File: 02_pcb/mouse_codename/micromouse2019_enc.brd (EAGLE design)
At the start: 5.9 x 11.1 mm, 7 parts, among them IC1 AS5047D

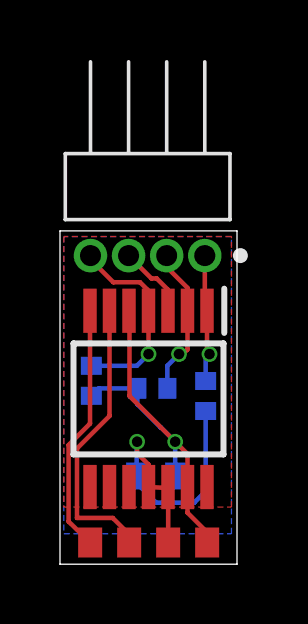
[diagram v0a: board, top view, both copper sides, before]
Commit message: ENC A B channels repaired
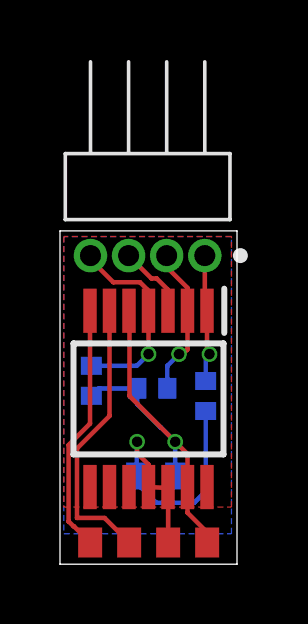
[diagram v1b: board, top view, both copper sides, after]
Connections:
- net A: now also IC1.7, PORT1.P1; no longer IC1.6, PORT1.P2
- net B: now also IC1.6, PORT1.P2; no longer IC1.7, PORT1.P1
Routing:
- net A: track 9.59 -> 8.33 mm
- net B: track 8.32 -> 9.43 mm
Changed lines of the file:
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@@
 <drawing>
 <settings>
-<setting alwaysvectorfont="no"/>
+<setting alwaysvectorfont="yes"/>
 <setting verticaltext="up"/>
 </settings>
@@
 </layers>
 <board>
-<fusionsync huburn="a.cGVyc29uYWw6dWUyOWUzYzUy" projecturn="a.cGVyc29uYWw6dWUyOWUzYzUyIzIwMTkwMjExMTc1NjcyODUx" f3durn="urn:adsk.wipprod:dm.lineage:Rxm10mLTRvSe4zHQ0xKiHA" pcbguid="812d53ff-404d-449c-89ab-42e65b23e1ef" lastpulledtime="" lastsyncedchangeguid="feedeed4-1ef2-0792-c0b8-603b07f8e484"/>
+<fusionsync huburn="a.cGVyc29uYWw6dWUyOWUzYzUy" projecturn="a.cGVyc29uYWw6dWUyOWUzYzUyIzIwMTkwMjExMTc1NjcyODUx" f3durn="urn:adsk.wipprod:dm.lineage:Rxm10mLTRvSe4zHQ0xKiHA" pcbguid="812d53ff-404d-449c-89ab-42e65b23e1ef" lastpulledtime="" lastsyncedchangeguid="d4eb9837-2cdc-5a8d-eec6-6bba6ad545ca"/>
 <plain>
 <wire x1="0" y1="11.11" x2="0" y2="0" width="0" layer="20"/>
@@
 <wire x1="4.90508125" y1="1.06391875" x2="4.90508125" y2="0.7232" width="0.1524" layer="1"/>
 </signal>
-<signal name="A">
+<signal name="B">
 <contactref element="IC1" pad="6"/>
 <wire x1="1.65" y1="8.448" x2="1.6510375" y2="4.94158125" width="0.1524" layer="1"/>
@@
 <wire x1="1.6510375" y1="4.94158125" x2="0.565978125" y2="3.856521875" width="0.1524" layer="1"/>
 <contactref element="PORT1" pad="P2"/>
-<wire x1="0.565978125" y1="1.54258125" x2="1.75941875" y2="1.54258125" width="0.1524" layer="1"/>
-<wire x1="2.30508125" y1="0.99691875" x2="2.30508125" y2="0.7232" width="0.1524" layer="1"/>
-<wire x1="1.75941875" y1="1.54258125" x2="2.30508125" y2="0.99691875" width="0.1524" layer="1"/>
+<wire x1="0.565978125" y1="1.54258125" x2="1.4857" y2="1.54258125" width="0.1524" layer="1"/>
+<wire x1="1.4857" y1="1.54258125" x2="2.30508125" y2="0.7232" width="0.1524" layer="1"/>
 </signal>
-<signal name="B">
+<signal name="A">
 <contactref element="IC1" pad="7"/>
 <wire x1="1" y1="8.448" x2="1.0010375" y2="4.68671875" width="0.1524" layer="1"/>
 <wire x1="1.0010375" y1="4.68671875" x2="0.286578125" y2="3.972259375" width="0.1524" layer="1"/>
+<wire x1="0.286578125" y1="3.972259375" x2="0.286578125" y2="1.42231875" width="0.1524" layer="1"/>
 <contactref element="PORT1" pad="P1"/>
-<wire x1="0.286578125" y1="1.42231875" x2="1.00508125" y2="0.7232" width="0.1524" layer="1"/>
-<wire x1="0.286578125" y1="3.972259375" x2="0.286578125" y2="1.42231875" width="0.1524" layer="1"/>
+<wire x1="0.286578125" y1="1.42231875" x2="0.2911" y2="1.42231875" width="0.1524" layer="1"/>
+<wire x1="0.2911" y1="1.42231875" x2="0.45024375" y2="1.263175" width="0.1524" layer="1"/>
+<wire x1="0.45024375" y1="1.263175" x2="0.46510625" y2="1.263175" width="0.1524" layer="1"/>
+<wire x1="0.46510625" y1="1.263175" x2="1.00508125" y2="0.7232" width="0.1524" layer="1"/>
 </signal>
 <signal name="CSN">

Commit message: module pcbs updated
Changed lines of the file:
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@@
 <drawing>
 <settings>
-<setting alwaysvectorfont="yes"/>
+<setting alwaysvectorfont="no"/>
 <setting verticaltext="up"/>
 </settings>
-<grid distance="2.5" unitdist="mil" unit="mil" style="lines" multiple="1" display="yes" altdistance="0.1" altunitdist="mil" altunit="mil"/>
+<grid distance="2.5" unitdist="mil" unit="mm" style="lines" multiple="1" display="yes" altdistance="0.1" altunitdist="mil" altunit="mil"/>
 <layers>
 <layer number="1" name="Top" color="4" fill="1" visible="yes" active="yes"/>
@@
 <layer number="14" name="Route14" color="22" fill="1" visible="no" active="no"/>
 <layer number="15" name="Route15" color="23" fill="1" visible="no" active="no"/>
-<layer number="16" name="Bottom" color="1" fill="1" visible="no" active="yes"/>
+<layer number="16" name="Bottom" color="1" fill="1" visible="yes" active="yes"/>
 <layer number="17" name="Pads" color="2" fill="1" visible="yes" active="yes"/>
 <layer number="18" name="Vias" color="2" fill="1" visible="yes" active="yes"/>
@@
 <layer number="20" name="Dimension" color="24" fill="1" visible="yes" active="yes"/>
 <layer number="21" name="tPlace" color="7" fill="1" visible="yes" active="yes"/>
-<layer number="22" name="bPlace" color="7" fill="1" visible="no" active="yes"/>
+<layer number="22" name="bPlace" color="7" fill="1" visible="yes" active="yes"/>
 <layer number="23" name="tOrigins" color="15" fill="1" visible="yes" active="yes"/>
 <layer number="24" name="bOrigins" color="15" fill="1" visible="no" active="yes"/>
 <layer number="25" name="tNames" color="7" fill="1" visible="yes" active="yes"/>
-<layer number="26" name="bNames" color="7" fill="1" visible="no" active="yes"/>
+<layer number="26" name="bNames" color="7" fill="1" visible="yes" active="yes"/>
 <layer number="27" name="tValues" color="7" fill="1" visible="yes" active="yes"/>
 <layer number="28" name="bValues" color="7" fill="1" visible="no" active="yes"/>
@@
 <dimension x1="2.95" y1="5.51" x2="0" y2="5.51" x3="1.475" y3="23.41" textsize="1.778" layer="47" dtype="horizontal" width="0.05" extwidth="0.01" extlength="2" precision="3"/>
 <dimension x1="5.9" y1="0" x2="5.9" y2="11.11" x3="11.58" y3="5.555" textsize="1.778" layer="47" dtype="horizontal" width="0.05" extwidth="0.01" extlength="2" precision="3"/>
-<text x="2.6289" y="7.0866" size="0.7112" layer="26" rot="R90">MISO</text>
-<text x="1.3589" y="7.0993" size="0.7112" layer="26" rot="R90">MOSI</text>
+<text x="2.5019" y="6.8326" size="0.8128" layer="26" rot="R90">MISO</text>
+<text x="1.4224" y="6.8453" size="0.8128" layer="26" rot="R90">MOSI</text>
 <text x="3.8989" y="7.6962" size="0.7112" layer="28" rot="R90">CLK</text>
-<text x="5.1689" y="7.5184" size="0.7112" layer="26" rot="R90">CSN</text>
+<text x="5.2324" y="7.2644" size="0.8128" layer="26" rot="R90">CSN</text>
+<text x="3.1115" y="7.3025" size="0.8128" layer="26" rot="MR90">CLK</text>
 </plain>
 <attributes>
@@
 <wire x1="2.9510375" y1="3.32058125" x2="2.5700375" y2="3.70158125" width="0.1524" layer="1"/>
 <wire x1="2.5700375" y1="3.70158125" x2="2.5700375" y2="4.08258125" width="0.1524" layer="1"/>
-<via x="2.5700375" y="4.08258125" extent="1-16" drill="0.35"/>
+<via x="2.5700375" y="4.08258125" extent="1-16" drill="0.3" diameter="0.6"/>
 <wire x1="2.5700375" y1="4.08258125" x2="2.5550375" y2="4.06758125" width="0.1524" layer="16"/>
 <wire x1="2.5550375" y1="4.06758125" x2="2.5550375" y2="2.93958125" width="0.1524" layer="16"/>
@@
 <wire x1="4.2510375" y1="7.16058125" x2="4.0940375" y2="7.00358125" width="0.1524" layer="1"/>
 <wire x1="4.0940375" y1="7.00358125" x2="3.9670375" y2="7.00358125" width="0.1524" layer="1"/>
-<via x="3.9670375" y="7.00358125" extent="1-16" drill="0.35"/>
+<via x="3.9670375" y="7.00358125" extent="1-16" drill="0.3" diameter="0.6"/>
 <wire x1="3.5780375" y1="5.86058125" x2="3.5780375" y2="6.61458125" width="0.1524" layer="16"/>
 <wire x1="3.5780375" y1="6.61458125" x2="3.9670375" y2="7.00358125" width="0.1524" layer="16"/>
@@
 <wire x1="2.3160375" y1="5.60658125" x2="2.3160375" y2="8.40258125" width="0.1524" layer="1"/>
 <wire x1="2.3160375" y1="8.40258125" x2="2.3" y2="8.448" width="0.1524" layer="1"/>
-<via x="3.8400375" y="4.08258125" extent="1-16" drill="0.35"/>
+<via x="3.8400375" y="4.08258125" extent="1-16" drill="0.3" diameter="0.6"/>
 <wire x1="2.5780375" y1="5.86058125" x2="1.2920375" y2="5.86058125" width="0.1524" layer="16"/>
 <wire x1="1.0460375" y1="5.61458125" x2="1.2920375" y2="5.86058125" width="0.1524" layer="16"/>
@@
 <wire x1="4.9" y1="8.448" x2="4.9010375" y2="7.08558125" width="0.1524" layer="1"/>
 <wire x1="4.9010375" y1="7.08558125" x2="4.9830375" y2="7.00358125" width="0.1524" layer="1"/>
-<via x="4.9830375" y="7.00358125" extent="1-16" drill="0.35"/>
+<via x="4.9830375" y="7.00358125" extent="1-16" drill="0.3" diameter="0.6"/>
 <wire x1="4.9830375" y1="7.00358125" x2="4.8560375" y2="6.87658125" width="0.1524" layer="16"/>
 <wire x1="4.8560375" y1="6.87658125" x2="4.8560375" y2="6.10658125" width="0.1524" layer="16"/>
@@
 <contactref element="R3" pad="2"/>
 <wire x1="2.95" y1="8.448" x2="2.9510375" y2="7.00358125" width="0.1524" layer="1"/>
-<via x="2.9510375" y="7.00358125" extent="1-16" drill="0.35"/>
+<via x="2.9510375" y="7.00358125" extent="1-16" drill="0.3" diameter="0.6"/>
 <wire x1="2.9510375" y1="7.00358125" x2="2.5620375" y2="6.61458125" width="0.1524" layer="16"/>
 <wire x1="2.5620375" y1="6.61458125" x2="1.0460375" y2="6.61458125" width="0.1524" layer="16"/>
